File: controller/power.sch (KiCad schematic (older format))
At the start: 21 parts, among them J22 BATT, Q8 NDT2955, U16 LM7805CT, U5 LM7805CT

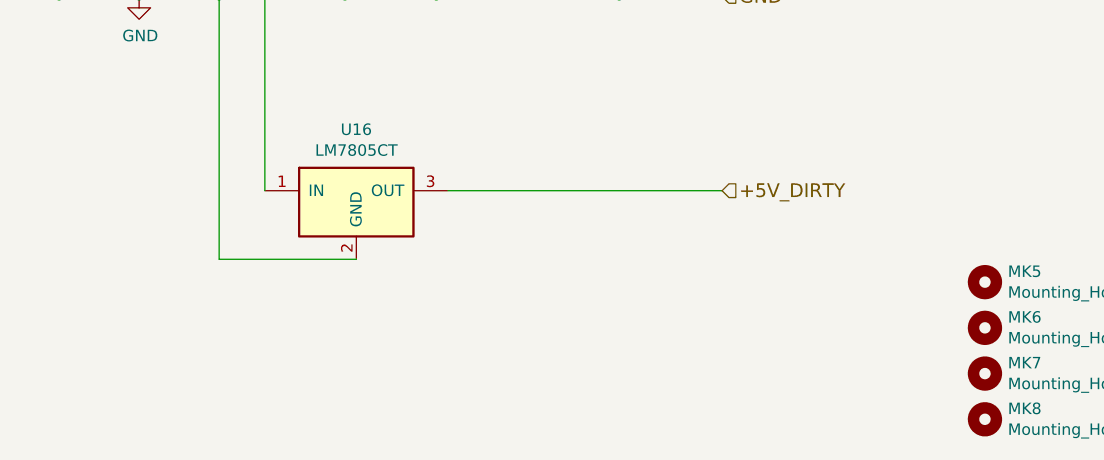
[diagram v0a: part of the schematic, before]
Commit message: add comments with fixes I had to make
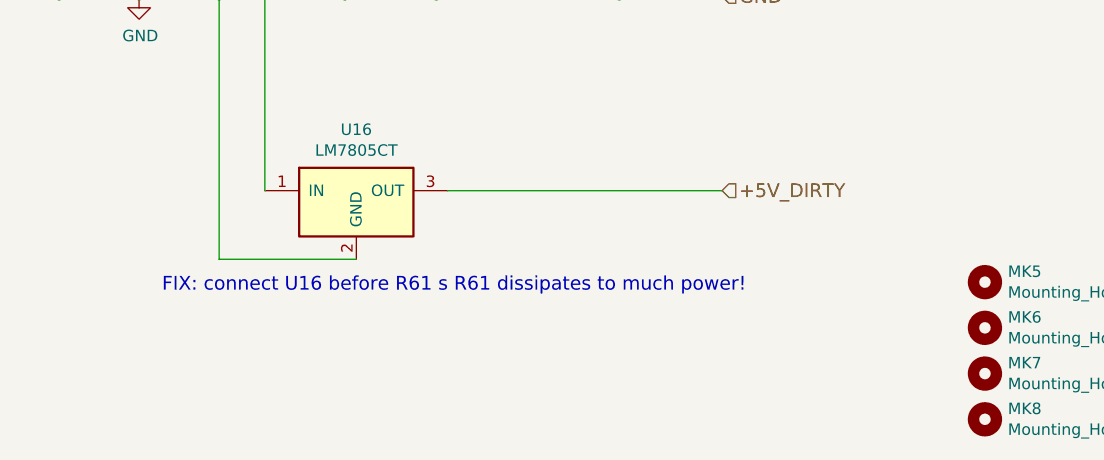
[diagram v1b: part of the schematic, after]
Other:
- note added: "FIX: connect U16 before R61 s R61 dissipates to much power!"
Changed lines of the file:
@@
 Text HLabel 8550 5100 2    60   Input ~ 0
 +5V_DIRTY
+Text Notes 6100 5550 0    60   ~ 0
+FIX: connect U16 before R61 s R61 dissipates to much power!
 $EndSCHEMATC
